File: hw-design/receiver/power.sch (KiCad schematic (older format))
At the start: 14 parts, among them P1 CONN_01X03, SW2 power, U5 MCP73833, U6 AP1117D33

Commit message: Skończona rewizja r1, wysłane do satlanfd
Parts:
- SW2: footprint w_switch:PCB_PUSH -> w_pin_strip:pin_socket_2; Opis (none) -> Włącznik zasilania, kołyskowy.
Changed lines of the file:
@@
 F 0 "SW2" H 6700 3225 50  0000 C CNN
 F 1 "power" H 6700 3300 50  0000 C CNN
-F 2 "w_switch:PCB_PUSH" H 6700 3125 60  0001 C CNN
-F 3 "" H 6700 3125 60  0000 C CNN
+F 2 "w_pin_strip:pin_socket_2" H 6700 3125 60  0001 C CNN
+F 3 "http://lispol.pl/product,2183,wylacznik_kolyskowy_mini_czarny.html" H 6700 3125 60  0001 C CNN
+F 4 "Włącznik zasilania, kołyskowy." H 6700 3125 60  0001 C CNN "Opis"
 	1    6700 3125
 	1    0    0    -1

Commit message: Revision 2
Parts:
- removed D3: LED, w_indicators:led_3mm_yellow, symbol LED
- removed D4: LED, w_indicators:led_3mm_green, symbol LED
- removed D5: LED, w_indicators:led_3mm_red, symbol LED
- removed R25, R26, R27: 730R, w_smd_resistors:r_0603, symbol R
- added P4, P5, P6: test-double, iwasz:testpad-2p, symbol test-double
- added Q4: BC847, w_smd_trans:sot23, symbol Q_NPN_BCE
- added Q5: NX7002AK, iwasz:sot23-pins123-ccw, symbol Q_NMOS_GSD
- added R33: 1k, w_smd_resistors:r_0603, symbol R
- added R34: 10k, w_smd_resistors:r_0603, symbol R
- C15, C16, C17: footprint w_smd_cap:c_tant_A -> w_smd_cap:c_tant_B
- P1: footprint w_conn_df13:df13-3p-125dsa -> w_pin_strip:pin_strip_3
- SW2: footprint w_pin_strip:pin_socket_2 -> w_pin_strip:pin_strip_2
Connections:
- net labels added: +BATT, complete, progress
- wire segments 46 -> 43
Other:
- moved on the sheet: C16, C17, P1, SW2, U6

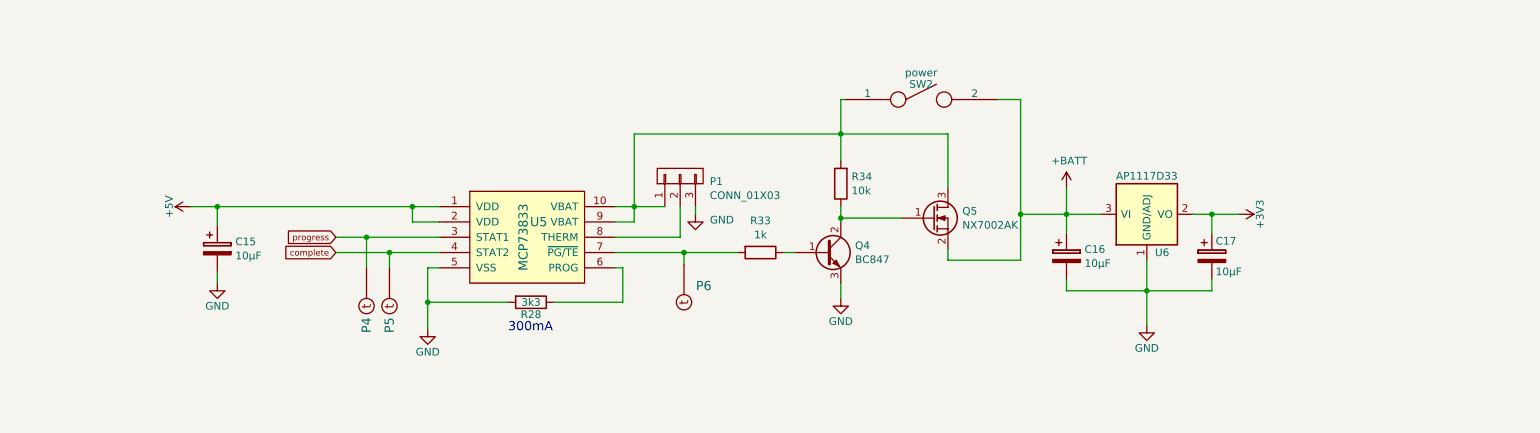
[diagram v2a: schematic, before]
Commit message: HW changes, removed BLE, and changed chanrging and ldo circuits
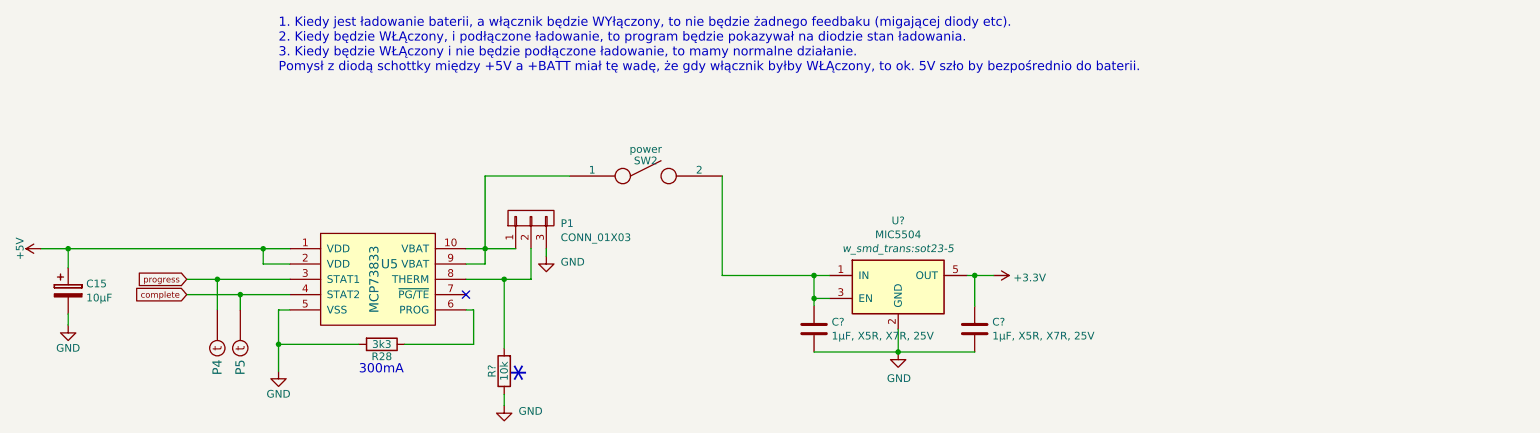
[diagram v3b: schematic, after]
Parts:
- removed C16, C17: 10µF, w_smd_cap:c_tant_B, symbol CP
- removed P6: test-double, iwasz:testpad-2p, symbol test-double
- removed Q4: BC847, w_smd_trans:sot23, symbol Q_NPN_BCE
- removed Q5: NX7002AK, iwasz:sot23-pins123-ccw, symbol Q_NMOS_GSD
- removed R33: 1k, w_smd_resistors:r_0603, symbol R
- removed R34: 10k, w_smd_resistors:r_0603, symbol R
- removed U6: AP1117D33, w_smd_trans:sot223, symbol AP1117D33
- added C? (x2): 1µF, X5R, X7R, 25V, w_smd_cap:c_0603, symbol C
- added R?: 10k, w_smd_resistors:r_0402, symbol R
- added U?: MIC5504, w_smd_trans:sot23-5, symbol TLV70012DDC
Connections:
- net +3V3: now also C?.1, U?.5 (OUT)
- net GND: now also C?.2, C?.2, R?.1, U?.2 (GND)
- net at P1.2 (P2), U5.8 (THERM): now also R?.2
- net +BATT: no longer names the net of SW2.2
- net +BATT: now also C?.1, U?.1 (IN), U?.3 (EN)
- no-connect marks 0 -> 1
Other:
- note added: "*"
- note added: "1. Kiedy jest ładowanie baterii, a włącznik będzie WYłączony, to nie będzie żadnego feedbaku (migającej diody etc). \n2. Kiedy będzie WŁĄczony, i podłączone ładowanie, to program będzie pokazywał na diodzie stan ładowania.\n3. Kiedy będzie WŁĄczony i nie będzie podłączone ładowanie, to mamy normalne działanie.\nPomysł z diodą schottky między +5V a +BATT miał tę wadę, że gdy włącznik byłby WŁĄczon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"
- moved on the sheet: C15, P1, P4, P5, R28, SW2, U5

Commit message: 2017 improvements
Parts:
- added R4, R5: 5k6, w_smd_resistors:r_0603, symbol R
- R2: renamed from R?; footprint w_smd_resistors:r_0402 -> w_smd_resistors:r_0603
- gave numbers to parts that had none: 3
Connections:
- net GND: now also R5.1
- net +BATT: now reaches C16.1, SW2.2, U6.1 (IN), U6.3 (EN)
- net +BATT: now also R4.2
- new net sense: R4.1, R5.2
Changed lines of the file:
@@
 $Descr A4 11693 8268
 encoding utf-8
-Sheet 2 2
+Sheet 2 3
 Title ""
 Date ""
@@
 	2425 3600 2425 3725
 $Comp
-L +5V #PWR028
+L +5V #PWR27
 U 1 1 56375D1B
 P 2250 3600
-F 0 "#PWR028" H 2250 3450 50  0001 C CNN
+F 0 "#PWR27" H 2250 3450 50  0001 C CNN
 F 1 "+5V" H 2250 3740 50  0000 C CNN
 F 2 "" H 2250 3600 60  0000 C CNN
@@
 Connection ~ 2425 3600
 $Comp
-L GND #PWR029
+L GND #PWR28
 U 1 1 56375D22
 P 2425 4100
-F 0 "#PWR029" H 2425 3850 50  0001 C CNN
+F 0 "#PWR28" H 2425 3850 50  0001 C CNN
 F 1 "GND" H 2425 3950 50  0000 C CNN
 F 2 "" H 2425 4100 60  0000 C CNN
@@
 Connection ~ 3700 3600
 Wire Wire Line
-	3200 3800 3875 3800
-Wire Wire Line
-	3200 3900 3875 3900
-$Comp
-L GND #PWR030
+	3300 3800 3875 3800
+Wire Wire Line
+	3300 3900 3875 3900
+$Comp
+L GND #PWR29
 U 1 1 56375D4C
 P 3800 4400
-F 0 "#PWR030" H 3800 4150 50  0001 C CNN
+F 0 "#PWR29" H 3800 4150 50  0001 C CNN
 F 1 "GND" H 3800 4250 50  0000 C CNN
 F 2 "" H 3800 4400 60  0000 C CNN
@@
 Connection ~ 5150 3600
 $Comp
-L GND #PWR033
+L GND #PWR31
 U 1 1 56375D84
 P 5550 3650
-F 0 "#PWR033" H 5550 3400 50  0001 C CNN
+F 0 "#PWR31" H 5550 3400 50  0001 C CNN
 F 1 "GND" H 5644 3613 50  0000 L CNN
 F 2 "" H 5550 3650 60  0000 C CNN
@@
 $EndComp
 Wire Wire Line
-	5450 3800 5025 3800
+	5025 3800 5450 3800
 $Comp
 L SPST SW2
@@
 	1    0    0    -1
 $EndComp
-Text GLabel 3200 3800 0    40   Input ~ 0
-progress
-Text GLabel 3200 3900 0    40   Input ~ 0
-complete
 $Comp
 L test-double P4
@@
 	5150 3125 5150 3700
 Wire Wire Line
-	5450 3600 5450 3800
+	5450 3800 5450 3600
 Wire Wire Line
 	5025 3600 5350 3600
@@
 	5550 3650 5550 3600
 $Comp
-L TLV70012DDC U?
+L TLV70012DDC U6
 U 1 1 58BD09B0
 P 7850 3825
-F 0 "U?" H 7850 4233 50  0000 C CNN
+F 0 "U6" H 7850 4233 50  0000 C CNN
 F 1 "MIC5504" H 7850 4142 50  0000 C CNN
 F 2 "w_smd_trans:sot23-5" H 7850 4051 50  0000 C CIN
@@
 $EndComp
 $Comp
-L GND #PWR?
+L GND #PWR34
 U 1 1 58BD09B4
 P 7850 4275
-F 0 "#PWR?" H 7850 4025 50  0001 C CNN
+F 0 "#PWR34" H 7850 4025 50  0001 C CNN
 F 1 "GND" H 7855 4102 50  0000 C CNN
 F 2 "" H 7850 4275 50  0000 C CNN
@@
 	7300 4275 8350 4275
 $Comp
-L C C?
+L C C16
 U 1 1 58BD09B7
 P 7300 4125
-F 0 "C?" H 7415 4171 50  0000 L CNN
+F 0 "C16" H 7415 4171 50  0000 L CNN
 F 1 "1µF, X5R, X7R, 25V" H 7415 4080 50  0000 L CNN
 F 2 "w_smd_cap:c_0603" H 7338 3975 50  0001 C CNN
@@
 $EndComp
 $Comp
-L C C?
+L C C17
 U 1 1 58BD09B8
 P 8350 4125
-F 0 "C?" H 8465 4171 50  0000 L CNN
+F 0 "C17" H 8465 4171 50  0000 L CNN
 F 1 "1µF, X5R, X7R, 25V" H 8465 4080 50  0000 L CNN
 F 2 "w_smd_cap:c_0603" H 8388 3975 50  0001 C CNN
@@
 $EndComp
 $Comp
-L +3.3V #PWR?
+L +3.3V #PWR35
 U 1 1 58BD09B9
 P 8475 3775
-F 0 "#PWR?" H 8475 3625 50  0001 C CNN
+F 0 "#PWR35" H 8475 3625 50  0001 C CNN
 F 1 "+3.3V" V 8490 3903 50  0000 L CNN
 F 2 "" H 8475 3775 50  0000 C CNN
@@
 1. Kiedy jest ładowanie baterii, a włącznik będzie WYłączony, to nie będzie żadnego feedbaku (migającej diody etc). \n2. Kiedy będzie WŁĄczony, i podłączone ładowanie, to program będzie pokazywał na diodzie stan ładowania.\n3. Kiedy będzie WŁĄczony i nie będzie podłączone ładowanie, to mamy normalne działanie.\nPomysł z diodą schottky między +5V a +BATT miał tę wadę, że gdy włącznik byłby WŁĄczony, to ok. 5V szło by bezpośrednio do baterii.
 $Comp
-L R R?
+L R R2
 U 1 1 58BD3A3D
 P 5275 4400
-F 0 "R?" V 5355 4400 50  0000 C CNN
+F 0 "R2" V 5355 4400 50  0000 C CNN
 F 1 "10k" V 5275 4400 50  0000 C CNN
-F 2 "w_smd_resistors:r_0402" V 5205 4400 30  0001 C CNN
+F 2 "w_smd_resistors:r_0603" V 5205 4400 30  0001 C CNN
 F 3 "" H 5275 4400 30  0000 C CNN
 	1    5275 4400
@@
 $EndComp
 $Comp
-L GND #PWR?
+L GND #PWR30
 U 1 1 58BD4121
 P 5275 4625
-F 0 "#PWR?" H 5275 4375 50  0001 C CNN
+F 0 "#PWR30" H 5275 4375 50  0001 C CNN
 F 1 "GND" H 5369 4588 50  0000 L CNN
 F 2 "" H 5275 4625 60  0000 C CNN
@@
 NoConn ~ 5025 3900
 Wire Wire Line
+	6875 3125 6700 3125
+Wire Wire Line
+	6700 3025 6700 3775
+Wire Wire Line
+	7300 3775 7300 3975
+Text HLabel 3300 3800 0    60   Output ~ 0
+progress
+Text HLabel 3300 3900 0    60   Output ~ 0
+complete
+$Comp
+L R R4
+U 1 1 58C05AB7
+P 7025 3125
+F 0 "R4" V 7105 3125 50  0000 C CNN
+F 1 "5k6" V 7025 3125 50  0000 C CNN
+F 2 "w_smd_resistors:r_0603" V 6955 3125 30  0001 C CNN
+F 3 "" H 7025 3125 30  0000 C CNN
+	1    7025 3125
+	0    1    1    0
+$EndComp
+$Comp
+L R R5
+U 1 1 58C05C11
+P 7450 3125
+F 0 "R5" V 7530 3125 50  0000 C CNN
+F 1 "5k6" V 7450 3125 50  0000 C CNN
+F 2 "w_smd_resistors:r_0603" V 7380 3125 30  0001 C CNN
+F 3 "" H 7450 3125 30  0000 C CNN
+	1    7450 3125
+	0    1    1    0
+$EndComp
+$Comp
+L GND #PWR33
+U 1 1 58C05C80
+P 7725 3125
+F 0 "#PWR33" H 7725 2875 50  0001 C CNN
+F 1 "GND" H 7819 3088 50  0000 L CNN
+F 2 "" H 7725 3125 60  0000 C CNN
+F 3 "" H 7725 3125 60  0000 C CNN
+	1    7725 3125
+	0    -1   -1   0
+$EndComp
+Wire Wire Line
+	7725 3125 7600 3125
+Wire Wire Line
+	7300 3125 7175 3125
+$Comp
+L +BATT #PWR32
+U 1 1 58C06D4A
+P 6700 3025
+F 0 "#PWR32" H 6700 2875 50  0001 C CNN
+F 1 "+BATT" H 6700 3165 50  0000 C CNN
+F 2 "" H 6700 3025 60  0000 C CNN
+F 3 "" H 6700 3025 60  0000 C CNN
+	1    6700 3025
+	1    0    0    -1
+$EndComp
+Wire Wire Line
 	5150 3125 5700 3125
-Wire Wire Line
-	6700 3125 6700 3775
-Wire Wire Line
-	7300 3775 7300 3975
+Connection ~ 6700 3125
+Text HLabel 7250 3000 1    60   Output ~ 0
+sense
+Wire Wire Line
+	7250 3125 7250 3000
+Connection ~ 7250 3125
 $EndSCHEMATC
